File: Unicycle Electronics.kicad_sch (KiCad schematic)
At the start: 20 parts, among them J1 USB_C, Q1 2N7002, SW1 INSERT PART NUMBER, SW2 INSERT PART NUMBER, U1 LDH-65-700, U2 ESP32-C6-MINI-1/U, U3 AMS1117-3.3

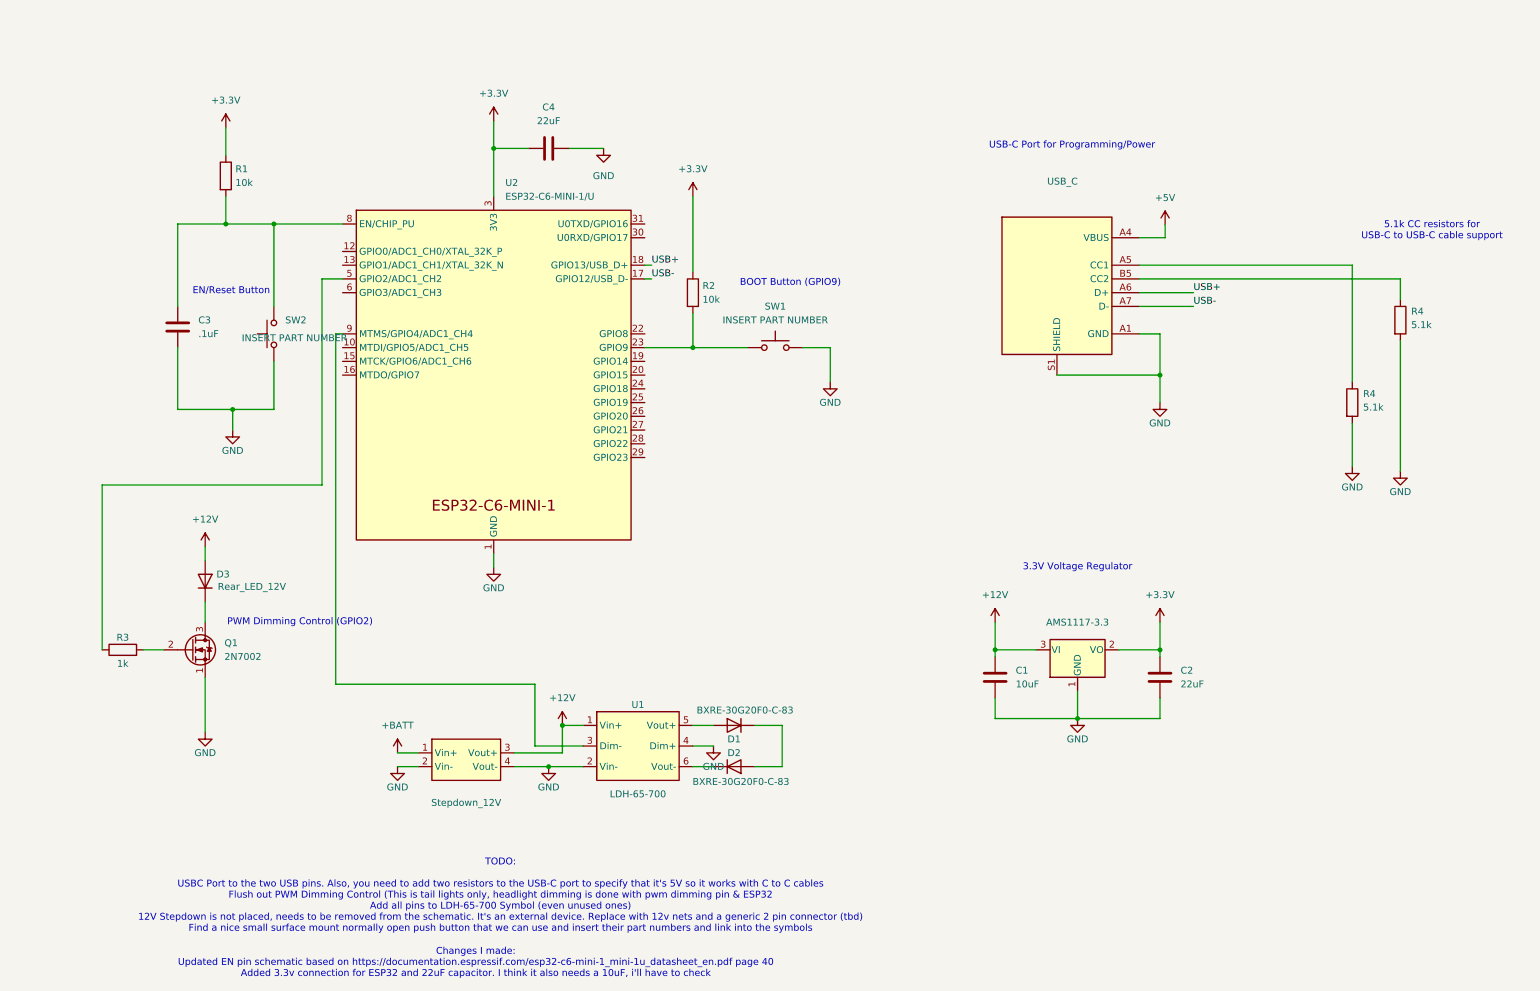
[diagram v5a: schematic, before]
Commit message: Schematic Update
Finished the TODO List
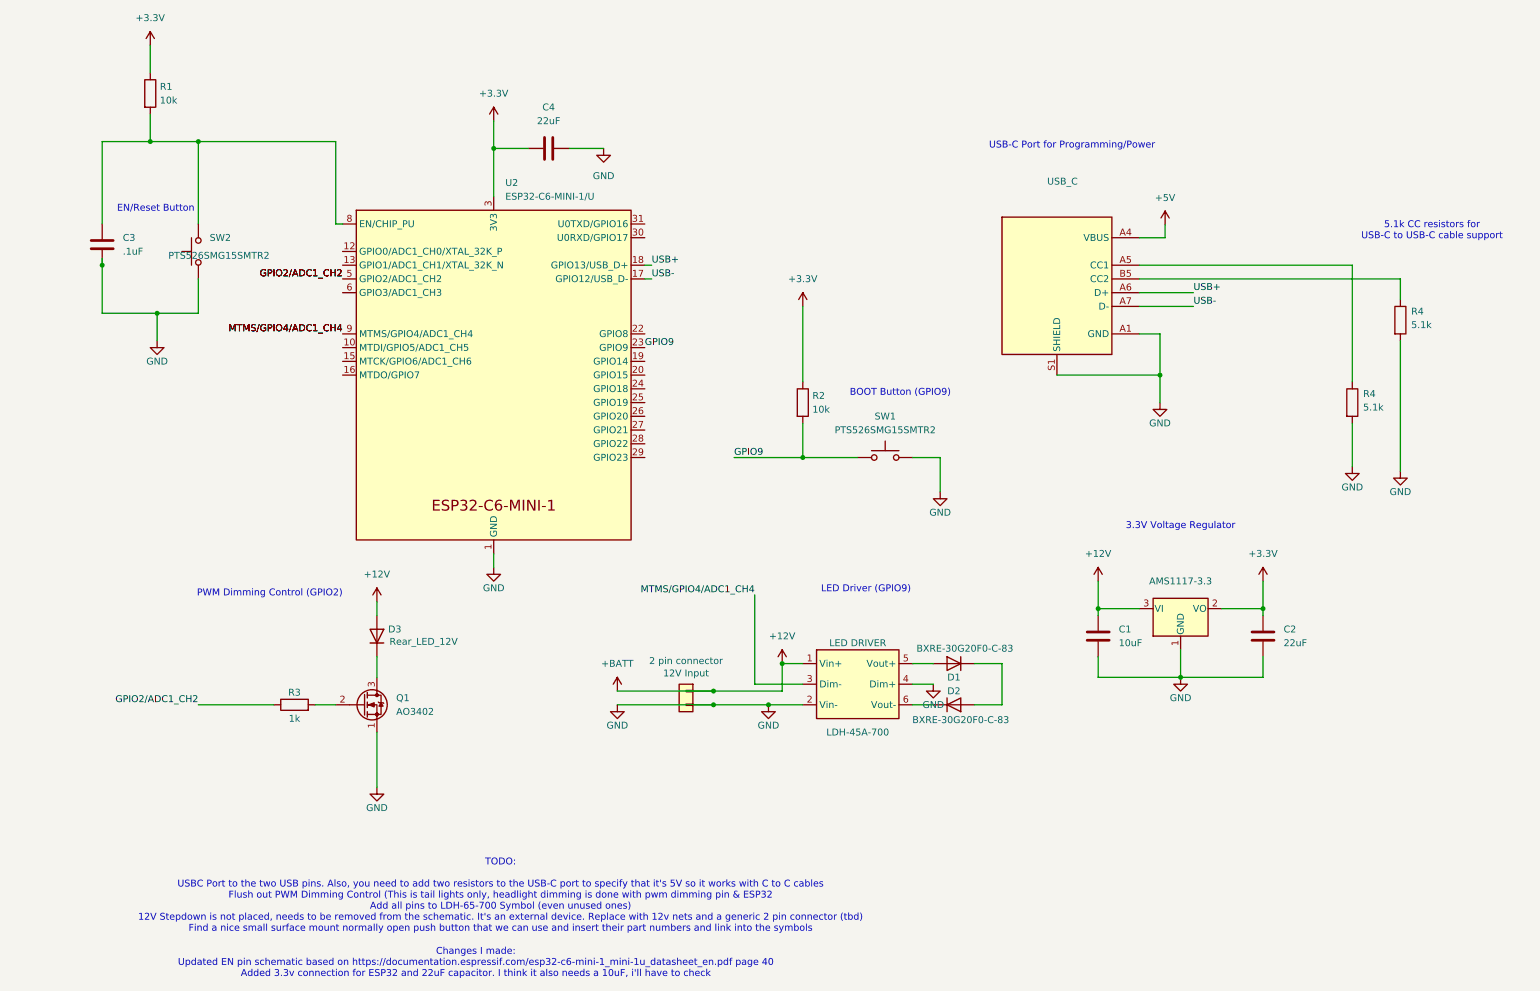
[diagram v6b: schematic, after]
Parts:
- removed U?: Stepdown_12V, symbol Converter_DCDC:DC_DC_Buck
- added 2 pin connector: 12V Input, symbol Connector_Generic:Conn_01x02
- LED DRIVER: renamed from U1; value LDH-65-700 -> LDH-45A-700
- Q1: value 2N7002 -> AO3402
- SW1, SW2: value INSERT PART NUMBER -> PTS526SMG15SMTR2
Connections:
- net +12V: now also 2 pin connector.1 (Pin_1)
- net GND: now also 2 pin connector.2 (Pin_2)
- net GPIO9: now reaches R2.2, SW1.1, U2.23 (GPIO9)
- net GPIO2/ADC1_CH2: now reaches R3.1, U2.5 (GPIO2/ADC1_CH2)
- net MTMS/GPIO4/ADC1_CH4: now reaches LED DRIVER.3 (Dim-), U2.9 (MTMS/GPIO4/ADC1_CH4)
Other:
- note added: "LED Driver (GPIO9)"
- moved on the sheet: C1, C2, C3, D1, D2, D3, LED DRIVER, Q1, R1, R2, R3, SW1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
